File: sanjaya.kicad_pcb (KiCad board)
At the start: 2 copper layers, 72 parts, among them J1 PWR_SUPPLY, J10 Bat_Bak_Byp_Gnd, J11 USB_B_Micro_OUT, J12 ON_Switch, J13 Raspberry_Pi_2_3, J14 Fan, J15 RS232, J16 RS485, J17 I2C, J18 Bat_Bak_Byp_Vcc, J2 Digital_Input_Signals, J3 Digital_Input_Gnd, J4 Screw_Terminal_01x03, J5 Screw_Terminal_01x03, J6 Analog_RSense, J7 Analog_420, J8 Supply_Safety_Bypass, J9 USB_B_Micro_IN, K1 Songle-SRD, K2 Songle-SRD, Q1 Q_PMOS_GSD, Q2 FDC021N30, SW2 SW_DIP_x04, U1 74HC14, U2 MCP9700T-ETT, U3 TPS2400BVR, U4 ULN2803A, U5 MCP3428, U6 TLP291-4, U7 MAX232, U8 SN65HVD75DR

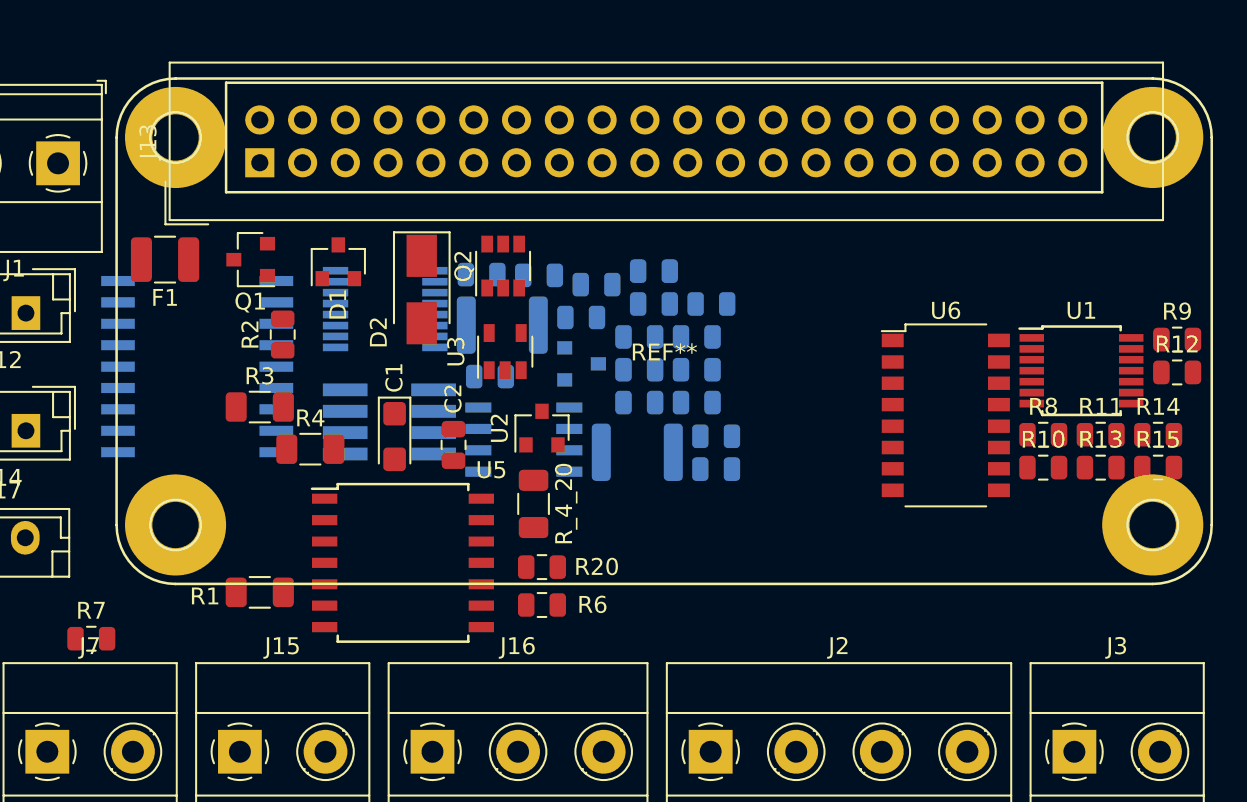
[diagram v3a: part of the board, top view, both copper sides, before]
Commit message: More layout done
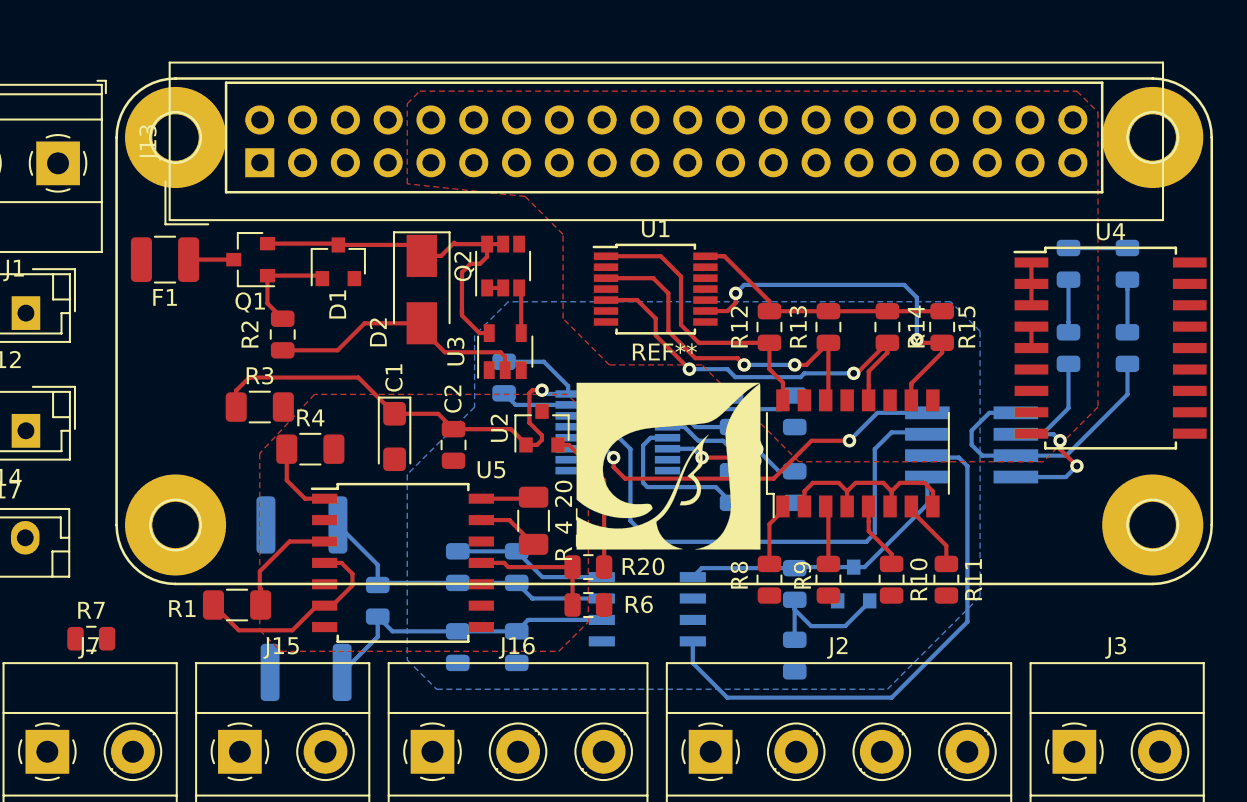
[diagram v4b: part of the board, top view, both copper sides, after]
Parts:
- added G***: LOGO, Custom Silkscreens:logo, F.Cu at (141.0, 107.5)
- added G***: LOGO, Custom Silkscreens:logo, B.Cu at (121.5, 101.2)
- U4: moved to F.Cu
- moved U4 54.2 mm to (167.2, 100.5)
- moved D_TX1 37.9 mm to (168.2, 100.5), turned to 90 degrees
- moved D_RX1 35.1 mm to (164.8, 100.5), turned to 90 degrees
- moved SW2 34.6 mm to (159.0, 106.2), turned to 180 degrees
- moved R_TX1 28.2 mm to (168.2, 95.5), turned to 270 degrees
- moved U1 25.7 mm to (140.2, 97.0)
- moved R9 25.1 mm to (150.5, 114.2), turned to 270 degrees
- moved R_RX1 24.6 mm to (164.8, 95.5), turned to 270 degrees
- moved R12 24.3 mm to (147.0, 99.2), turned to 90 degrees
- moved F3 23.6 mm to (119.5, 119.8)
- moved R19 21.6 mm to (123.8, 115.5), turned to 270 degrees
- moved D3 20.8 mm to (152.0, 114.5), turned to 90 degrees
- moved C10 19.9 mm to (132.0, 118.2), turned to 270 degrees
- moved R18 19.7 mm to (128.5, 118.2), turned to 270 degrees
- moved R8 18.4 mm to (147.0, 114.2), turned to 270 degrees
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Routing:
- net /3V3: track 0.00 -> 72.7 mm, vias 0 -> 1
- net Net-(SW2-Pad6): track 0.00 -> 32.2 mm
- net Net-(SW2-Pad7): track 0.00 -> 32.0 mm
- net Net-(SW2-Pad8): track 0.00 -> 24.0 mm, vias 0 -> 2
- net Net-(R14-Pad1): track 0.00 -> 23.9 mm, vias 0 -> 2
- net Net-(D1-Pad1): track 0.00 -> 22.1 mm
- net Net-(R15-Pad1): track 0.00 -> 22.1 mm, vias 0 -> 2
- net Net-(R13-Pad1): track 0.00 -> 20.7 mm, vias 0 -> 2
- net Net-(C9-Pad2): track 0.00 -> 18.3 mm
- net Net-(C10-Pad1): track 0.00 -> 18.1 mm
- net Net-(D3-Pad1): track 0.00 -> 17.3 mm
- net Net-(R12-Pad1): track 0.00 -> 17.3 mm
- net /rPi/UART_TX: track 0.00 -> 16.7 mm
- net /powerSupply/Gnd_In: track 0.00 -> 15.7 mm
- net /rPi/UART_RX: track 0.00 -> 15.0 mm, vias 0 -> 2
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- added copper zone on F.Cu, net /AGND
- added copper zone on B.Cu, net /DGND
- added copper zone on F.Cu, net /DGND

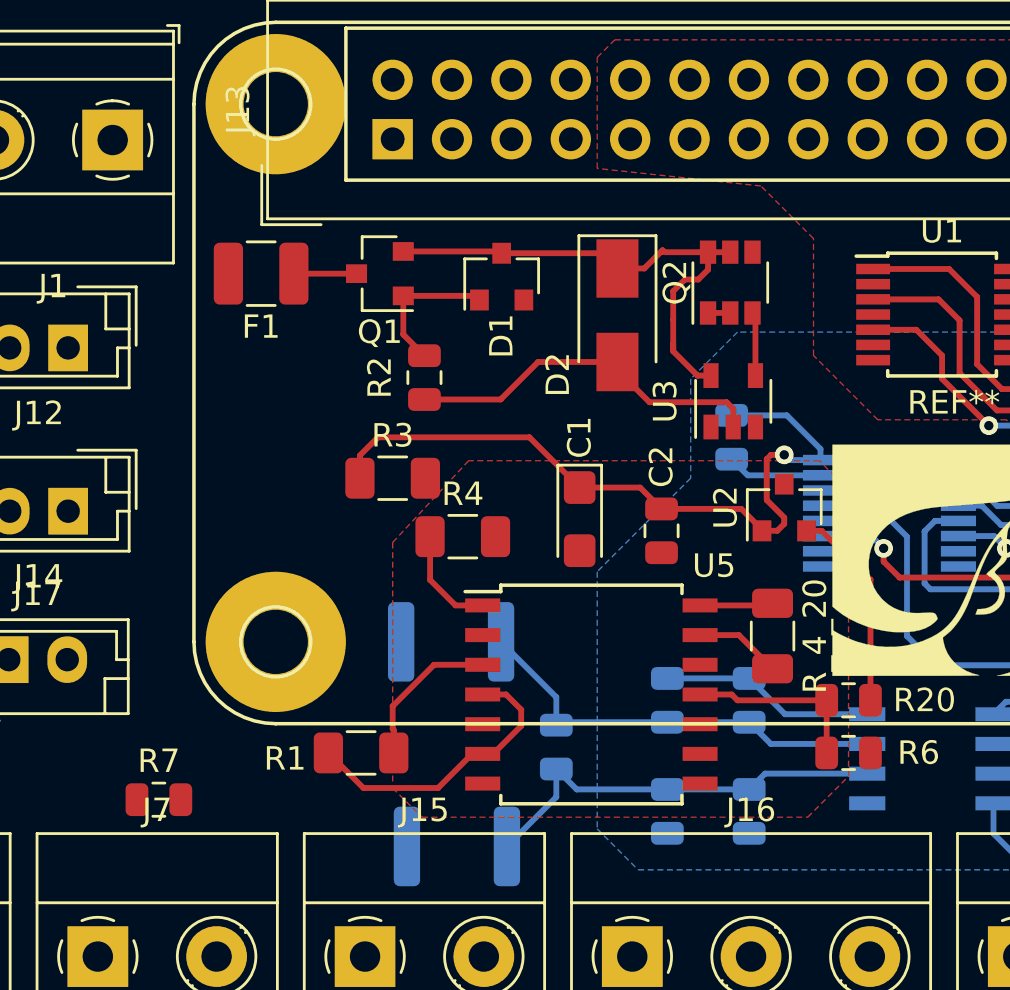
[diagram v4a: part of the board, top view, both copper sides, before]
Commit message: Changes: 1. Added a power LED 2. Added PPTC to the inputs of optocoupler 3. Added PPTC to the transceiver side of the RS232 driver 4. Corrected ADC footprint
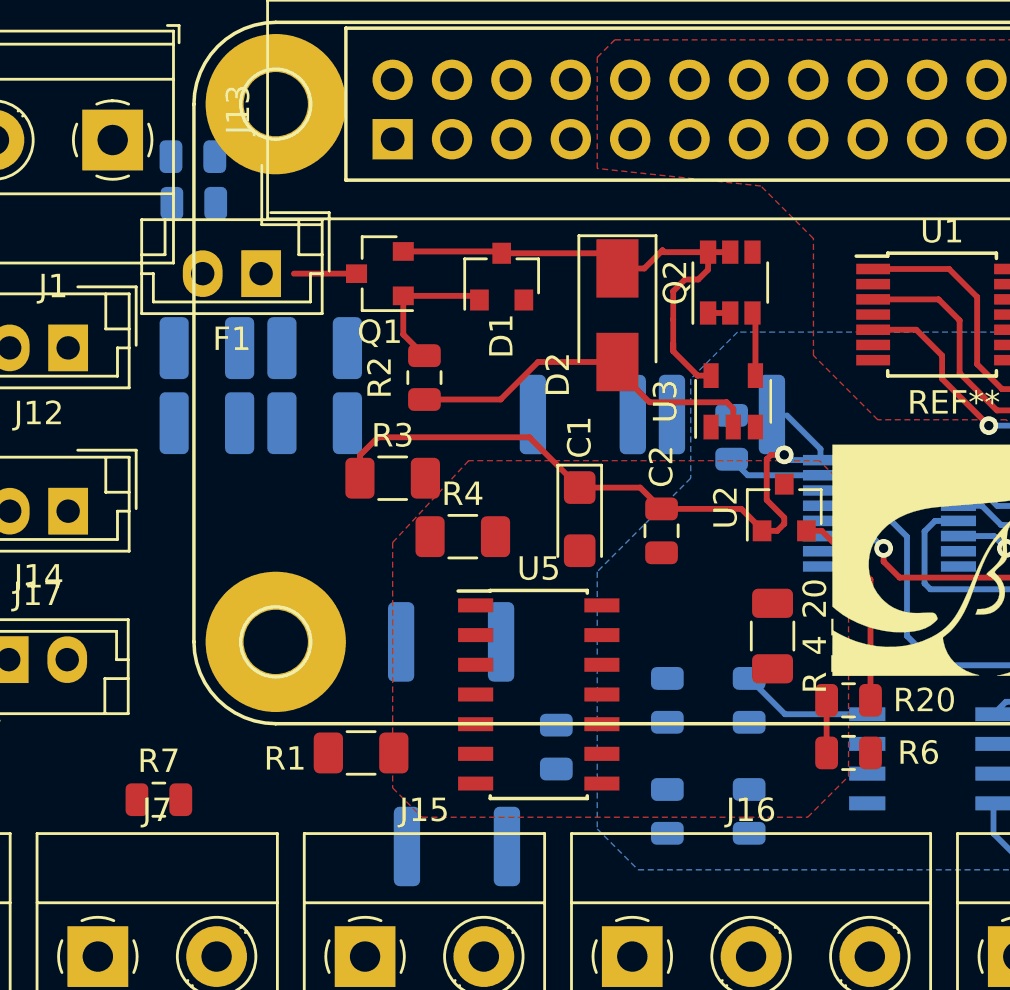
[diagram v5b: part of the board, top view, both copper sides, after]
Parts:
- added D4: PWR_LED, LED_SMD:LED_0805_2012Metric, B.Cu at (108.2, 92.2)
- added F4: PPTC_500mA, Fuse:Fuse_1812_4532Metric, B.Cu at (124.9, 101.3)
- added F5: PPTC_500mA, Fuse:Fuse_1812_4532Metric, B.Cu at (130.8, 101.3)
- added F6: PPTC_50mA, Fuse:Fuse_1210_3225Metric, B.Cu at (108.8, 101.6)
- added F7: PPTC_50mA, Fuse:Fuse_1210_3225Metric, B.Cu at (108.8, 98.4)
- added F8: PPTC_50mA, Fuse:Fuse_1210_3225Metric, B.Cu at (113.4, 101.6)
- added F9: PPTC_50mA, Fuse:Fuse_1210_3225Metric, B.Cu at (113.4, 98.4)
- added R5: 330, Resistor_SMD:R_0805_2012Metric, B.Cu at (108.2, 90.2)
- D1: value 10V -> Zener_10V
- D2: value 24V -> Zener_24V
- F1: value 3A -> GlassFuse_3A; footprint Fuse:Fuse_1210_3225Metric -> Connector_JST:JST_EH_B02B-EH-A_1x02_P2.50mm_Vertical
- F2, F3: value PPTC -> PPTC_500mA
- U5: footprint Package_SO:SOIC-14W_7.5x9.0mm_P1.27mm -> Package_SO:SOIC-14_3.9x8.7mm_P1.27mm
- moved U5 2.25 mm to (123.0, 113.2)
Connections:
- R10 pad 2: /digitalSensing/Vin_3 -> Net-(F8-Pad1)
- R11 pad 2: /digitalSensing/Vin_4 -> Net-(F9-Pad1)
- R8 pad 2: /digitalSensing/Vin_1 -> Net-(F6-Pad1)
- R9 pad 2: /digitalSensing/Vin_2 -> Net-(F7-Pad1)
- U7 pad 13: /serial/RS232_RX -> Net-(F5-Pad2)
- U7 pad 14: /serial/RS232_TX -> Net-(F4-Pad2)
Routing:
- net /3V3: track 72.7 -> 54.2 mm
- net Net-(C9-Pad2): track 18.3 -> 0.00 mm
- net Net-(C10-Pad1): track 18.1 -> 0.00 mm
- net /3V3_Net+: track 6.60 -> 0.00 mm
- net Net-(R20-Pad1): track 7.77 -> 2.25 mm
- net Net-(R3-Pad2): track 4.55 -> 0.00 mm
- net /analogSensing/420+: track 3.70 -> 0.00 mm
- net /analogSensing/420-: track 3.14 -> 0.00 mm

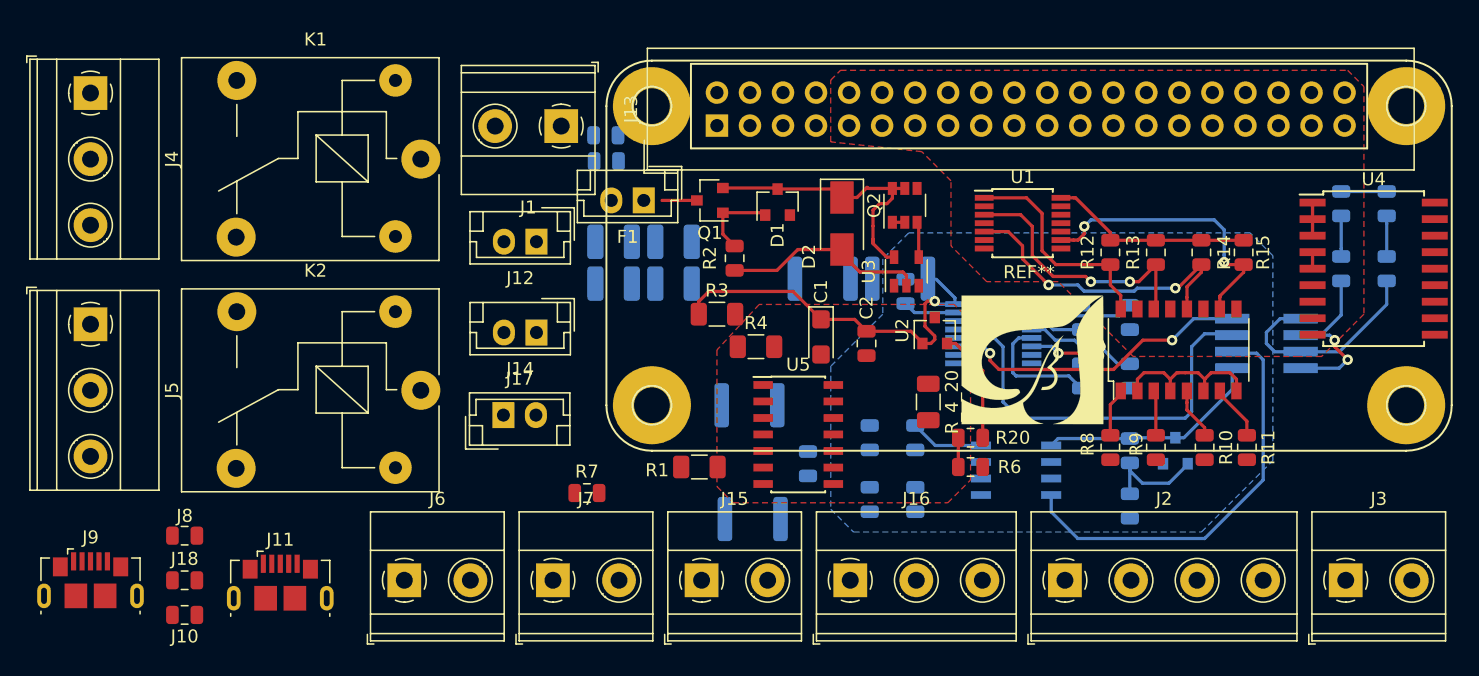
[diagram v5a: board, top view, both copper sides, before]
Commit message: Screw connectors footprint changed to 2.54mm ones and relayout done for all terminal blocks
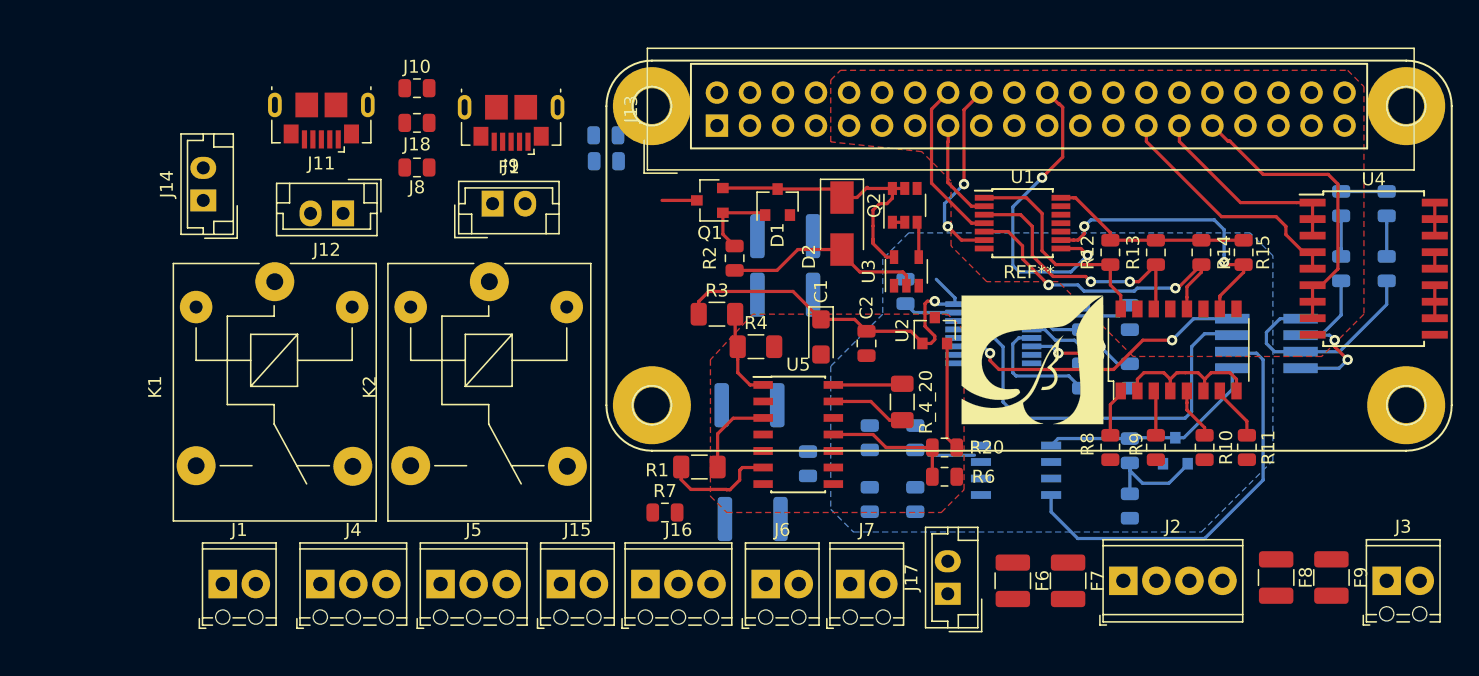
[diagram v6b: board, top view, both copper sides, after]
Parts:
- F6, F7, F8, F9: moved to F.Cu
- J1, J15, J3, J6, J7: footprint TerminalBlock_Phoenix:TerminalBlock_Phoenix_MKDS-1,5-2-5.08_1x02_P5.08mm_Horizontal -> TerminalBlock_Phoenix:TerminalBlock_Phoenix_MPT-0,5-2-2.54_1x02_P2.54mm_Horizontal
- J16, J4, J5: footprint TerminalBlock_Phoenix:TerminalBlock_Phoenix_MKDS-1,5-3-5.08_1x03_P5.08mm_Horizontal -> TerminalBlock_Phoenix:TerminalBlock_Phoenix_MPT-0,5-3-2.54_1x03_P2.54mm_Horizontal
- J2: footprint TerminalBlock_Phoenix:TerminalBlock_Phoenix_MKDS-1,5-4-5.08_1x04_P5.08mm_Horizontal -> TerminalBlock_Phoenix:TerminalBlock_Phoenix_MPT-0,5-4-2.54_1x04_P2.54mm_Horizontal
- moved F9 56.8 mm to (164.0, 124.2), turned to 270 degrees
- moved F8 51.6 mm to (159.8, 124.2), turned to 270 degrees
- moved J9 47.8 mm to (100.9, 89.3), turned to 180 degrees
- moved J10 44.3 mm to (93.7, 86.6), turned to 0 degrees
- moved J1 43.8 mm to (78.8, 124.8), turned to 0 degrees
- moved F7 43.6 mm to (143.8, 124.5), turned to 270 degrees
- moved J4 41.7 mm to (86.2, 124.8), turned to 0 degrees
- moved J18 39.4 mm to (93.7, 89.3), turned to 180 degrees
- moved F6 38.3 mm to (139.5, 124.5), turned to 270 degrees
- moved J17 36.8 mm to (134.5, 125.5), turned to 90 degrees
- moved J11 35.7 mm to (86.3, 89.1), turned to 180 degrees
- moved J5 33.5 mm to (95.5, 124.8), turned to 0 degrees
- moved J8 33.5 mm to (93.7, 92.7), turned to 0 degrees
- moved J6 27.8 mm to (120.5, 124.8)
- moved J14 27.6 mm to (77.2, 95.2), turned to 90 degrees
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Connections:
- J13 pad 27: (no net) -> /actuation/Fan_Ctrl
- J13 pad 7: /actuation/Fan_Ctrl -> (no net)
- J14 pad 1: /rPi/5V_In -> Net-(J14-Pad1)
- J14 pad 2: Net-(J14-Pad2) -> /rPi/5V_In
- U4 pad 14: Net-(J14-Pad2) -> Net-(J14-Pad1)
- U4 pad 15: Net-(J14-Pad2) -> Net-(J14-Pad1)
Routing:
- net /D_INPUT_D: track 0.00 -> 24.2 mm, vias 0 -> 2
- net /actuation/Relay2_Ctrl: track 0.00 -> 23.0 mm
- net /actuation/Fan_Ctrl: track 1.27 -> 19.2 mm
- net /D_INPUT_C: track 0.00 -> 14.8 mm, vias 0 -> 2
- net /actuation/Relay1_Ctrl: track 2.54 -> 15.9 mm
- net /D_INPUT_B: track 0.00 -> 12.8 mm
- net Net-(R20-Pad1): track 2.25 -> 10.3 mm
- net /D_INPUT_A: track 0.00 -> 7.94 mm
- net Net-(R3-Pad2): track 0.00 -> 6.92 mm
- net /3V3: track 54.2 -> 60.8 mm
- net /3V3_Net+: track 0.00 -> 6.56 mm
- net /analogSensing/420+: track 0.00 -> 5.90 mm
- net /analogSensing/420-: track 0.00 -> 5.34 mm
- net Net-(K2-Pad5): track 0.00 -> 2.54 mm
- net Net-(K1-Pad2): track 0.00 -> 2.54 mm
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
